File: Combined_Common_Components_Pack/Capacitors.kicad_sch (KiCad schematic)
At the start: 19 parts

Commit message: Added some connectors and basic parts
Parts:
- added C52: 1nF, Capacitor_SMD:C_0805_2012Metric, symbol Device:C
- added C53: 10nF, Capacitor_SMD:C_0805_2012Metric, symbol Device:C
- added C54: 100nF, Capacitor_SMD:C_0805_2012Metric, symbol Device:C
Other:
- note added: "Basic 0402 10% Capacitors"
- moved on the sheet: C11, C12, C14, C17, C18, C19, C3, C7, C8, C9

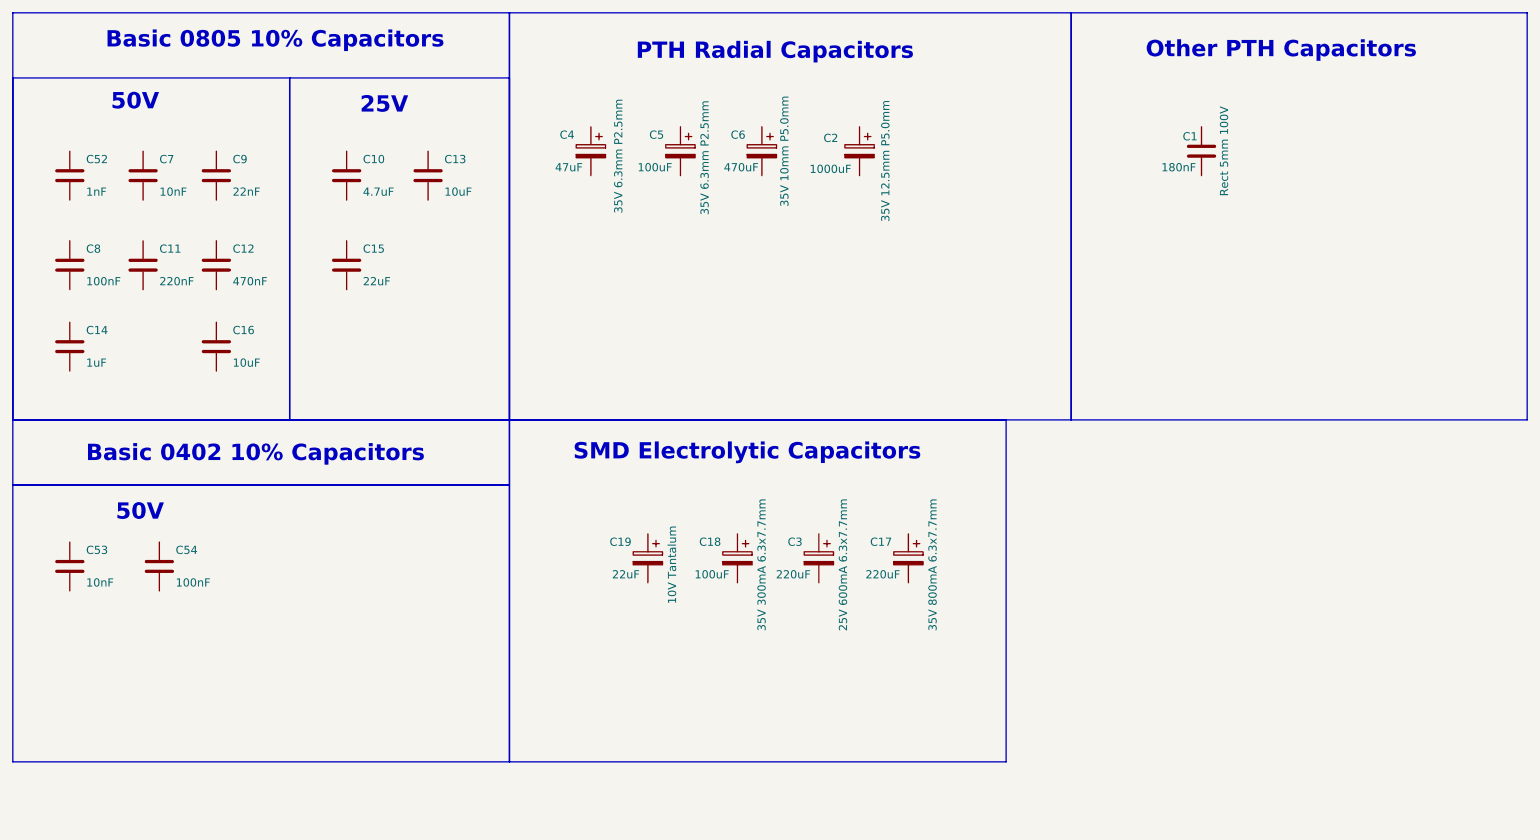
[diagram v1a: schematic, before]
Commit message: Minor updates
Basically components annotation, and more basic parts added
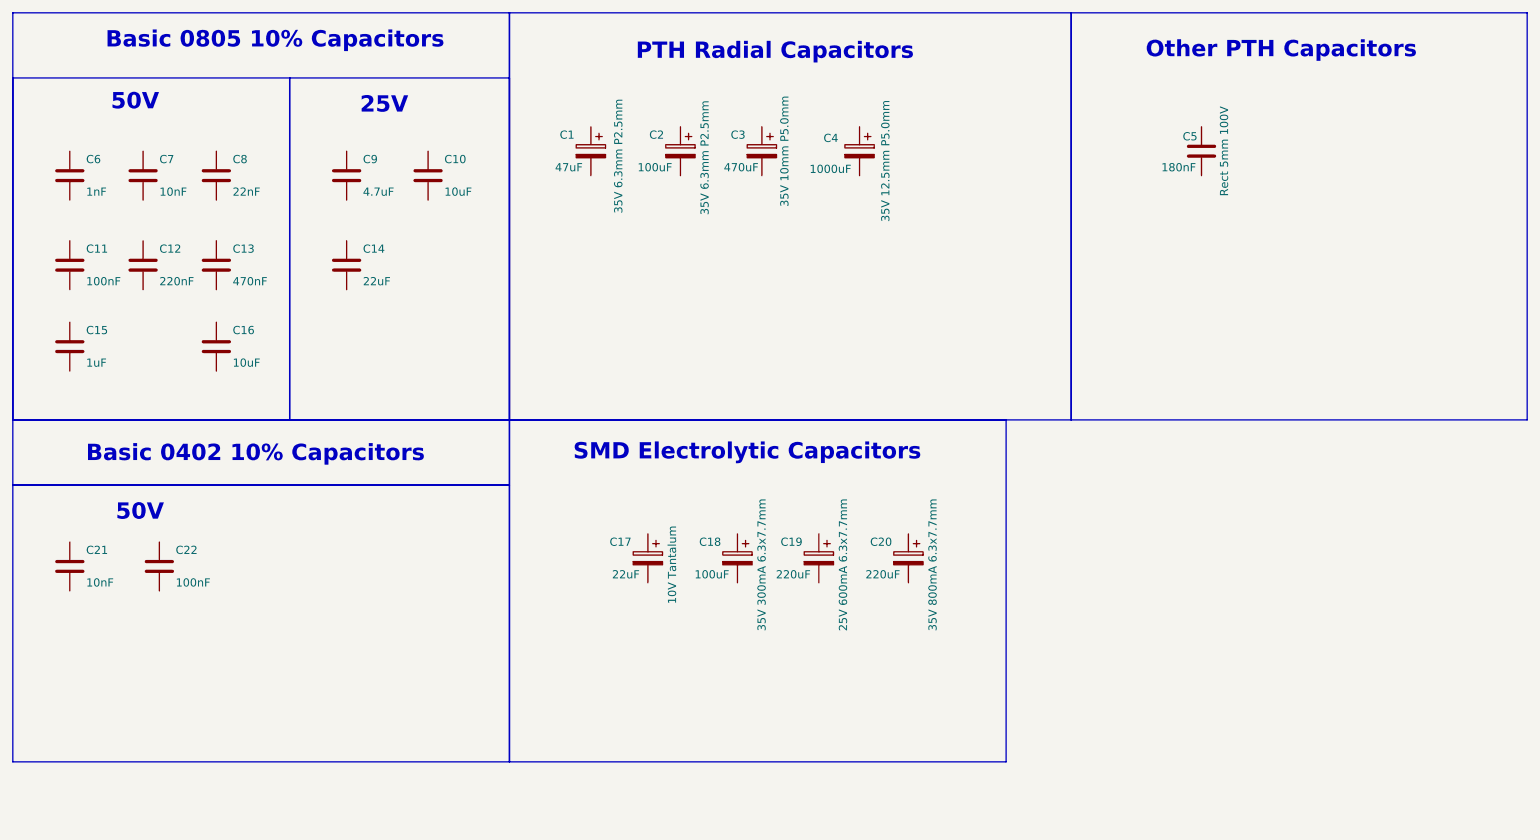
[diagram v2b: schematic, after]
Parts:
- renumbered C4 to C1, C13 to C10, C8 to C11, C11 to C12, C12 to C13, C15 to C14, C14 to C15, C19 to C17, C3 to C19, C5 to C2, C17 to C20, C53 to C21, C54 to C22, C6 to C3, C2 to C4, C1 to C5, C52 to C6, C9 to C8, C10 to C9
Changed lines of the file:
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@@
 		(on_board yes)
 		(dnp no)
-		(property "Reference" "C52"
+		(property "Reference" "C6"
 			(at 44.45 45.72 0)
 			(effects
@@
 			(project "Combined_Common_Components_Pack"
 				(path "/59e42e8e-5444-465a-b7a8-ffbd342a8d49/5d66c02b-43c6-47cc-adf8-9e937eddf5c2"
-					(reference "C52")
+					(reference "C6")
 					(unit 1)
 				)
@@
 		(on_board yes)
 		(dnp no)
-		(property "Reference" "C54"
+		(property "Reference" "C22"
 			(at 58.42 106.68 0)
 			(effects
@@
 			(project "Combined_Common_Components_Pack"
 				(path "/59e42e8e-5444-465a-b7a8-ffbd342a8d49/5d66c02b-43c6-47cc-adf8-9e937eddf5c2"
-					(reference "C54")
+					(reference "C22")
 					(unit 1)
 				)
@@
 		(on_board yes)
 		(dnp no)
-		(property "Reference" "C17"
+		(property "Reference" "C20"
 			(at 170.18 105.41 0)
 			(effects
@@
 			(project "Combined_Common_Components_Pack"
 				(path "/59e42e8e-5444-465a-b7a8-ffbd342a8d49/5d66c02b-43c6-47cc-adf8-9e937eddf5c2"
-					(reference "C17")
+					(reference "C20")
 					(unit 1)
 				)
@@
 		(on_board yes)
 		(dnp no)
-		(property "Reference" "C14"
+		(property "Reference" "C15"
 			(at 44.45 72.39 0)
 			(effects
@@
 			(project "Combined_Common_Components_Pack"
 				(path "/59e42e8e-5444-465a-b7a8-ffbd342a8d49/5d66c02b-43c6-47cc-adf8-9e937eddf5c2"
-					(reference "C14")
+					(reference "C15")
 					(unit 1)
 				)
@@
 		(on_board yes)
 		(dnp no)
-		(property "Reference" "C10"
+		(property "Reference" "C9"
 			(at 87.63 45.72 0)
 			(effects
@@
 			(project "Combined_Common_Components_Pack"
 				(path "/59e42e8e-5444-465a-b7a8-ffbd342a8d49/5d66c02b-43c6-47cc-adf8-9e937eddf5c2"
-					(reference "C10")
+					(reference "C9")
 					(unit 1)
 				)
@@
 		(on_board yes)
 		(dnp no)
-		(property "Reference" "C9"
+		(property "Reference" "C8"
 			(at 67.31 45.72 0)
 			(effects
@@
 			(project "Combined_Common_Components_Pack"
 				(path "/59e42e8e-5444-465a-b7a8-ffbd342a8d49/5d66c02b-43c6-47cc-adf8-9e937eddf5c2"
-					(reference "C9")
+					(reference "C8")
 					(unit 1)
 				)
@@
 		(on_board yes)
 		(dnp no)
-		(property "Reference" "C5"
+		(property "Reference" "C2"
 			(at 134.62 41.91 0)
 			(effects
@@
 			(project "Combined_Common_Components_Pack"
 				(path "/59e42e8e-5444-465a-b7a8-ffbd342a8d49/5d66c02b-43c6-47cc-adf8-9e937eddf5c2"
-					(reference "C5")
+					(reference "C2")
 					(unit 1)
 				)
@@
 		(on_board yes)
 		(dnp no)
-		(property "Reference" "C15"
+		(property "Reference" "C14"
 			(at 87.63 59.69 0)
 			(effects
@@
 			(project "Combined_Common_Components_Pack"
 				(path "/59e42e8e-5444-465a-b7a8-ffbd342a8d49/5d66c02b-43c6-47cc-adf8-9e937eddf5c2"
-					(reference "C15")
+					(reference "C14")
 					(unit 1)
 				)
@@
 		(on_board yes)
 		(dnp no)
-		(property "Reference" "C4"
+		(property "Reference" "C1"
 			(at 120.65 41.91 0)
 			(effects
@@
 			(project "Combined_Common_Components_Pack"
 				(path "/59e42e8e-5444-465a-b7a8-ffbd342a8d49/5d66c02b-43c6-47cc-adf8-9e937eddf5c2"
-					(reference "C4")
+					(reference "C1")
 					(unit 1)
 				)
@@
 		(on_board yes)
 		(dnp no)
-		(property "Reference" "C13"
+		(property "Reference" "C10"
 			(at 100.33 45.72 0)
 			(effects
@@
 			(project "Combined_Common_Components_Pack"
 				(path "/59e42e8e-5444-465a-b7a8-ffbd342a8d49/5d66c02b-43c6-47cc-adf8-9e937eddf5c2"
-					(reference "C13")
+					(reference "C10")
 					(unit 1)
 				)
@@
 		(on_board yes)
 		(dnp no)
-		(property "Reference" "C12"
+		(property "Reference" "C13"
 			(at 67.31 59.69 0)
 			(effects
@@
 			(project "Combined_Common_Components_Pack"
 				(path "/59e42e8e-5444-465a-b7a8-ffbd342a8d49/5d66c02b-43c6-47cc-adf8-9e937eddf5c2"
-					(reference "C12")
+					(reference "C13")
 					(unit 1)
 				)
@@
 		(on_board yes)
 		(dnp no)
-		(property "Reference" "C11"
+		(property "Reference" "C12"
 			(at 55.88 59.69 0)
 			(effects
@@
 			(project "Combined_Common_Components_Pack"
 				(path "/59e42e8e-5444-465a-b7a8-ffbd342a8d49/5d66c02b-43c6-47cc-adf8-9e937eddf5c2"
-					(reference "C11")
+					(reference "C12")
 					(unit 1)
 				)
@@
 		(on_board yes)
 		(dnp no)
-		(property "Reference" "C19"
+		(property "Reference" "C17"
 			(at 129.54 105.41 0)
 			(effects
@@
 			(project "Combined_Common_Components_Pack"
 				(path "/59e42e8e-5444-465a-b7a8-ffbd342a8d49/5d66c02b-43c6-47cc-adf8-9e937eddf5c2"
-					(reference "C19")
+					(reference "C17")
 					(unit 1)
 				)
@@
 		(on_board yes)
 		(dnp no)
-		(property "Reference" "C3"
+		(property "Reference" "C19"
 			(at 156.21 105.41 0)
 			(effects
@@
 			(project "Combined_Common_Components_Pack"
 				(path "/59e42e8e-5444-465a-b7a8-ffbd342a8d49/5d66c02b-43c6-47cc-adf8-9e937eddf5c2"
-					(reference "C3")
+					(reference "C19")
 					(unit 1)
 				)
@@
 		(on_board yes)
 		(dnp no)
-		(property "Reference" "C8"
+		(property "Reference" "C11"
 			(at 44.45 59.69 0)
 			(effects
@@
 			(project "Combined_Common_Components_Pack"
 				(path "/59e42e8e-5444-465a-b7a8-ffbd342a8d49/5d66c02b-43c6-47cc-adf8-9e937eddf5c2"
-					(reference "C8")
+					(reference "C11")
 					(unit 1)
 				)
@@
 		(on_board yes)
 		(dnp no)
-		(property "Reference" "C1"
+		(property "Reference" "C5"
 			(at 216.662 42.164 0)
 			(effects
@@
 			(project "Combined_Common_Components_Pack"
 				(path "/59e42e8e-5444-465a-b7a8-ffbd342a8d49/5d66c02b-43c6-47cc-adf8-9e937eddf5c2"
-					(reference "C1")
+					(reference "C5")
 					(unit 1)
 				)
@@
 		(on_board yes)
 		(dnp no)
-		(property "Reference" "C6"
+		(property "Reference" "C3"
 			(at 147.32 41.91 0)
 			(effects
@@
 			(project "Combined_Common_Components_Pack"
 				(path "/59e42e8e-5444-465a-b7a8-ffbd342a8d49/5d66c02b-43c6-47cc-adf8-9e937eddf5c2"
-					(reference "C6")
+					(reference "C3")
 					(unit 1)
 				)
@@
 		(on_board yes)
 		(dnp no)
-		(property "Reference" "C53"
+		(property "Reference" "C21"
 			(at 44.45 106.68 0)
 			(effects
@@
 			(project "Combined_Common_Components_Pack"
 				(path "/59e42e8e-5444-465a-b7a8-ffbd342a8d49/5d66c02b-43c6-47cc-adf8-9e937eddf5c2"
-					(reference "C53")
+					(reference "C21")
 					(unit 1)
 				)
@@
 		(on_board yes)
 		(dnp no)
-		(property "Reference" "C2"
+		(property "Reference" "C4"
 			(at 161.798 42.418 0)
 			(effects
@@
 			(project "Combined_Common_Components_Pack"
 				(path "/59e42e8e-5444-465a-b7a8-ffbd342a8d49/5d66c02b-43c6-47cc-adf8-9e937eddf5c2"
-					(reference "C2")
+					(reference "C4")
 					(unit 1)
 				)

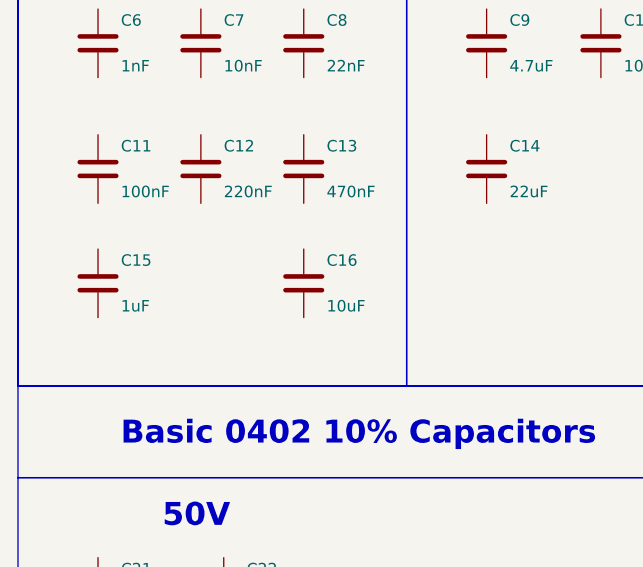
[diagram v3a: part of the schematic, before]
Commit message: Added XL4001 Load limiter devboard
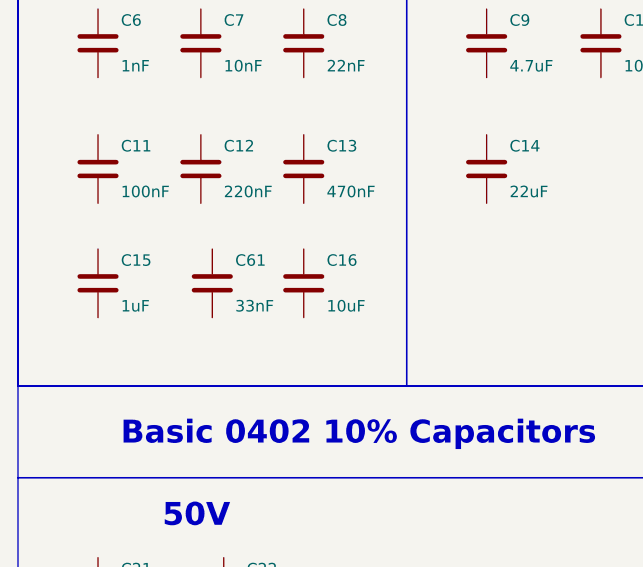
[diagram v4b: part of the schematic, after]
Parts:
- added C61: 33nF, Capacitor_SMD:C_0805_2012Metric, symbol Device:C
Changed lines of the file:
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@@
+	(symbol
+		(lib_id "Device:C")
+		(at 54.61 74.93 0)
+		(unit 1)
+		(exclude_from_sim no)
+		(in_bom yes)
+		(on_board yes)
+		(dnp no)
+		(property "Reference" "C61"
+			(at 57.15 72.39 0)
+			(effects
+				(font
+					(size 1.27 1.27)
+				)
+				(justify left)
+			)
+		)
+		(property "Value" "33nF"
+			(at 57.15 77.47 0)
+			(effects
+				(font
+					(size 1.27 1.27)
+				)
+				(justify left)
+			)
+		)
+		(property "Footprint" "Capacitor_SMD:C_0805_2012Metric"
+			(at 55.5752 78.74 0)
+			(effects
+				(font
+					(size 1.27 1.27)
+				)
+				(hide yes)
+			)
+		)
+		(property "Datasheet" "https://www.lcsc.com/datasheet/C1729.pdf"
+			(at 54.61 74.93 0)
+			(effects
+				(font
+					(size 1.27 1.27)
+				)
+				(hide yes)
+			)
+		)
+		(property "Description" "33nF ±10% 50V Ceramic Capacitor X7R 0805"
+			(at 54.61 74.93 0)
+			(effects
+				(font
+					(size 1.27 1.27)
+				)
+				(hide yes)
+			)
+		)
+		(property "LCSC" "C107150"
+			(at 54.61 74.93 0)
+			(effects
+				(font
+					(size 1.27 1.27)
+				)
+				(hide yes)
+			)
+		)
+		(property "Manufacturer " "YAGEO"
+			(at 54.61 74.93 0)
+			(effects
+				(font
+					(size 1.27 1.27)
+				)
+				(hide yes)
+			)
+		)
+		(property "Mfr. Part Number" "CC0805KRX7R9BB333"
+			(at 54.61 74.93 0)
+			(effects
+				(font
+					(size 1.27 1.27)
+				)
+				(hide yes)
+			)
+		)
+		(property "Observations" "Accepts other suppliers"
+			(at 54.61 74.93 0)
+			(effects
+				(font
+					(size 1.27 1.27)
+				)
+				(hide yes)
+			)
+		)
+		(pin "1"
+		)
+		(pin "2"
+		)
+		(instances
+			(project "Combined_Common_Components_Pack"
+				(path "/59e42e8e-5444-465a-b7a8-ffbd342a8d49/5d66c02b-43c6-47cc-adf8-9e937eddf5c2"
+					(reference "C61")
+					(unit 1)
+				)
+			)
+		)
+	)
 	(symbol
 		(lib_id "Device:C")
